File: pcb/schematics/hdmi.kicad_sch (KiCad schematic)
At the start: 24 parts

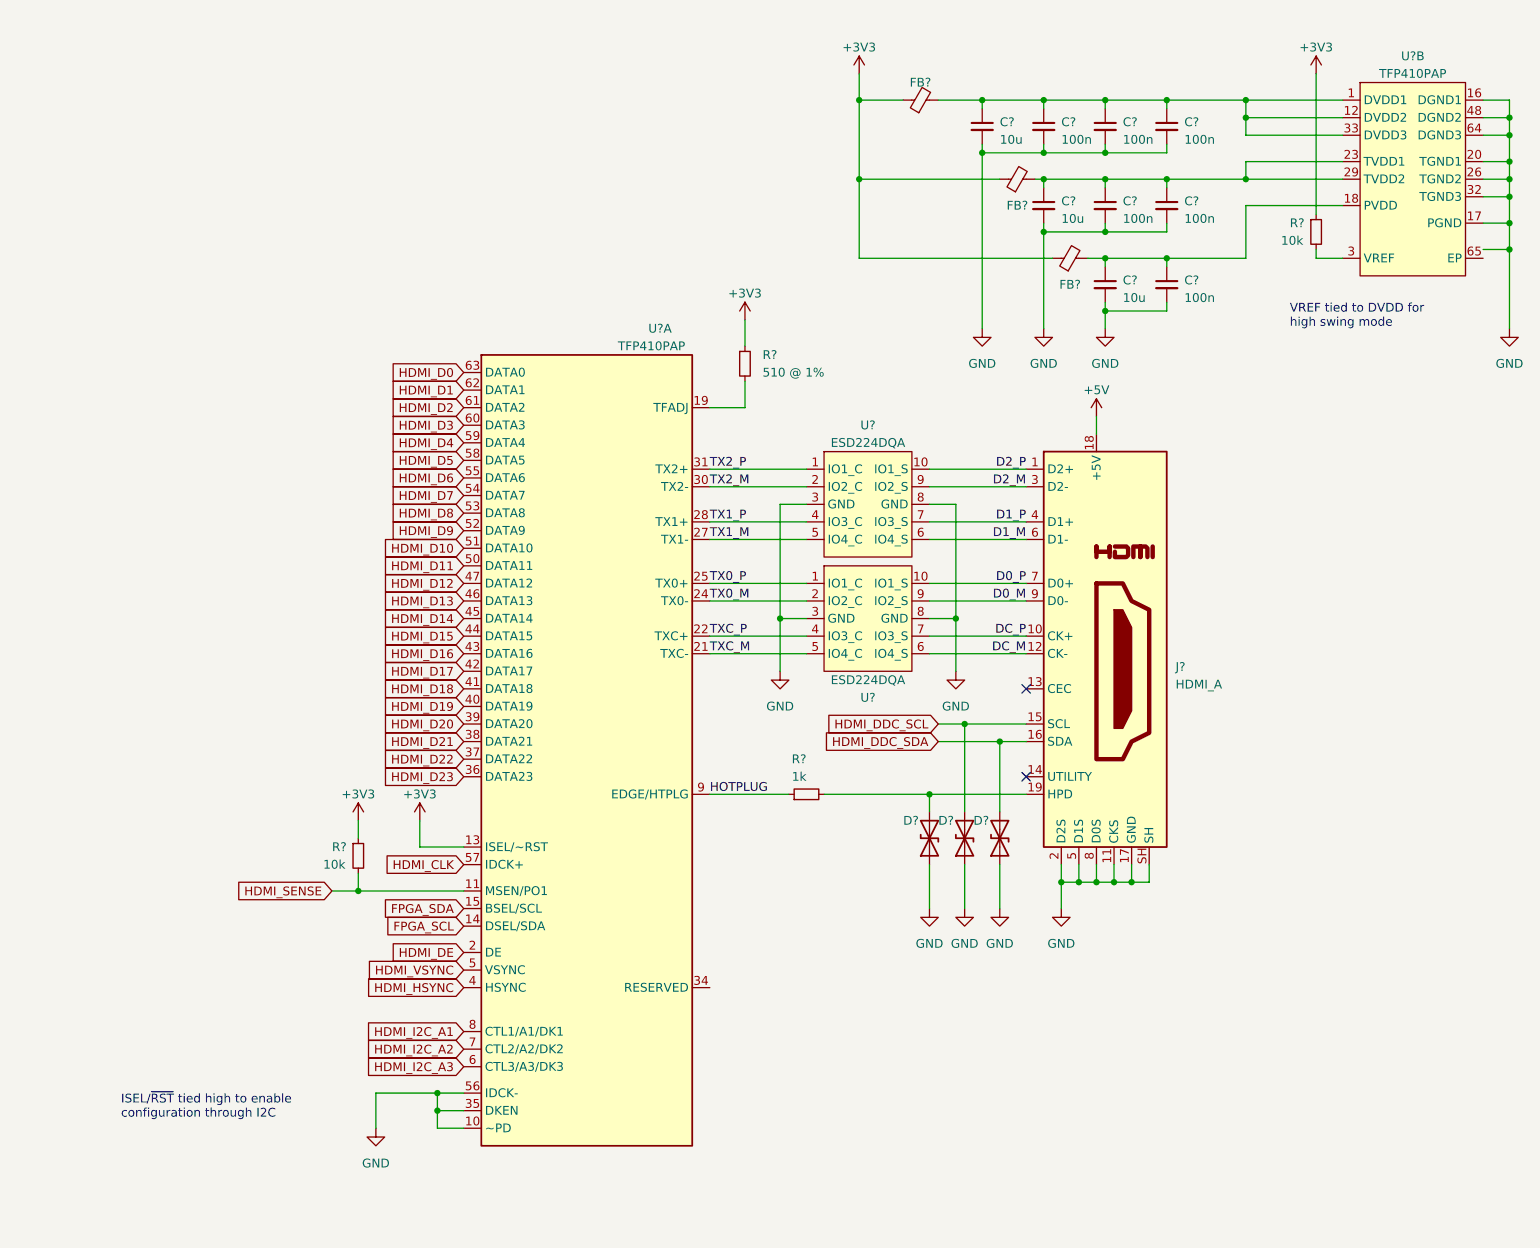
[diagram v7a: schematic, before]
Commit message: choose components and add footprints
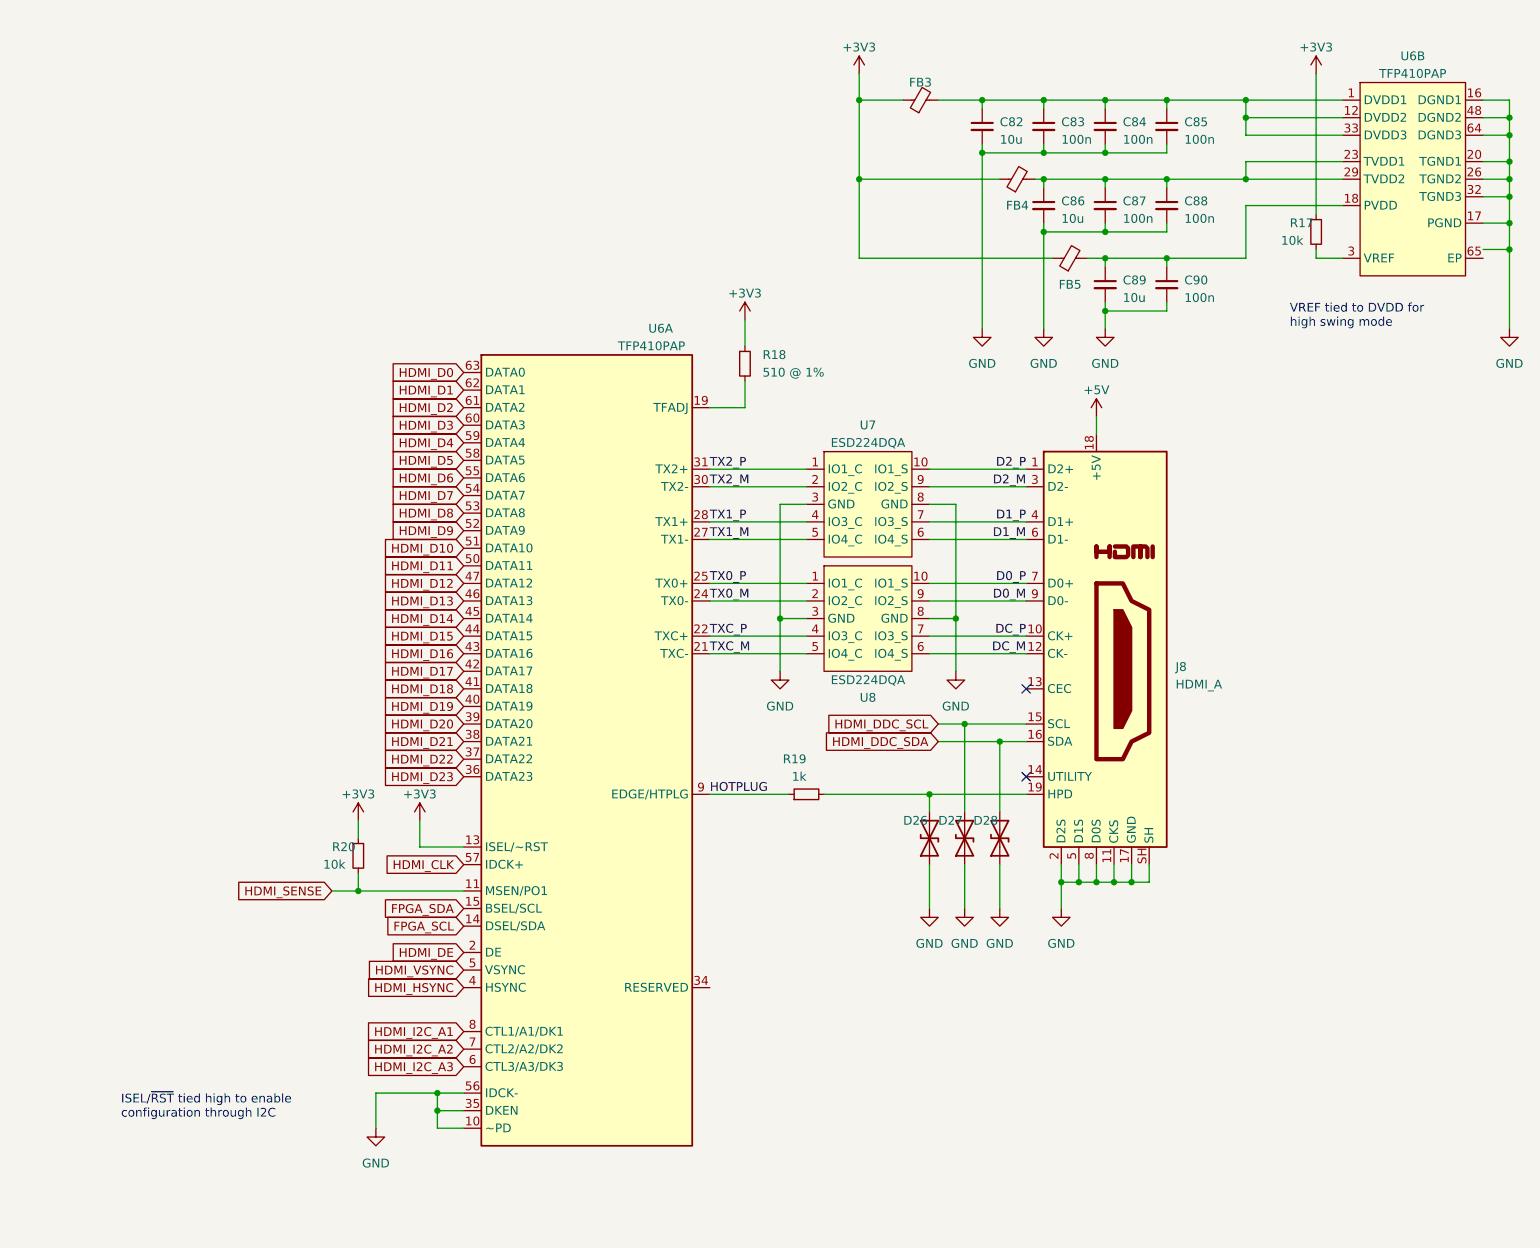
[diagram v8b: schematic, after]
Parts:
- C82, C86, C89: renamed from C?; footprint (none) -> Capacitor_SMD:C_0805_2012Metric; Part Number (none) -> JMK212ABJ106MG-T
- C83, C84, C85, C87, C88, C90: renamed from C?; footprint (none) -> Capacitor_SMD:C_0603_1608Metric; Part Number (none) -> EMK107B7104KA-T
- D26, D27, D28: renamed from D?; footprint (none) -> Diode_SMD:D_0603_1608Metric; Part Number (none) -> 82356240030
- FB3, FB4, FB5: renamed from FB?; footprint (none) -> Inductor_SMD:L_0805_2012Metric; Part Number (none) -> MFBM1V2012-150-R
- J8: renamed from J?; footprint (none) -> RAHHD19TR:RAAHD19TR; Part Number (none) -> RAHHD19TR
- R17, R20: renamed from R?; footprint (none) -> Resistor_SMD:R_0603_1608Metric; Part Number (none) -> RC0603JR-0710KL
- R18: renamed from R?; footprint (none) -> Resistor_SMD:R_0603_1608Metric; Part Number (none) -> RC0603FR-07510RL
- R19: renamed from R?; footprint (none) -> Resistor_SMD:R_0603_1608Metric; Part Number (none) -> CRCW06031K00JNEB
- U6: renamed from U?; Part Number (none) -> TFP410PAP
- U7, U8: renamed from U?; footprint (none) -> ESD224DQA:IC_TPD4EUSB30DQAR; Part Number (none) -> ESD224DQA
